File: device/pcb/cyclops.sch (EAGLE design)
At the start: 193 parts, among them Q1 NDS351AN, Q2 NDS351AN, Q3 NDS351AN, Q4 IRF510, U1 MCP4921, U10 LT1880, U11 ZXTD, U12 DG9421, U13 THS4281, U14 ZXTD, U15 MAX4564, U16 OPA1664, U2 LT1764A, U3 BD00FC0WEFJ, U4 LTM8020, U5 LT1931, U6 TPS72325, U7 TLV3701, U8 LT1711, U9 ADR03

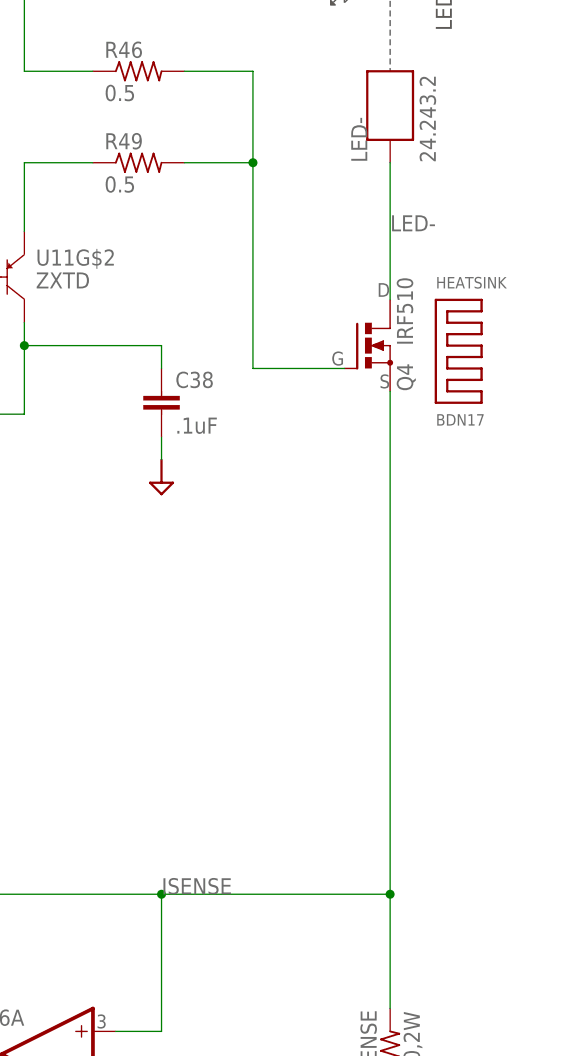
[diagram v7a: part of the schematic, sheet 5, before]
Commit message: Thermal fixes after testing.
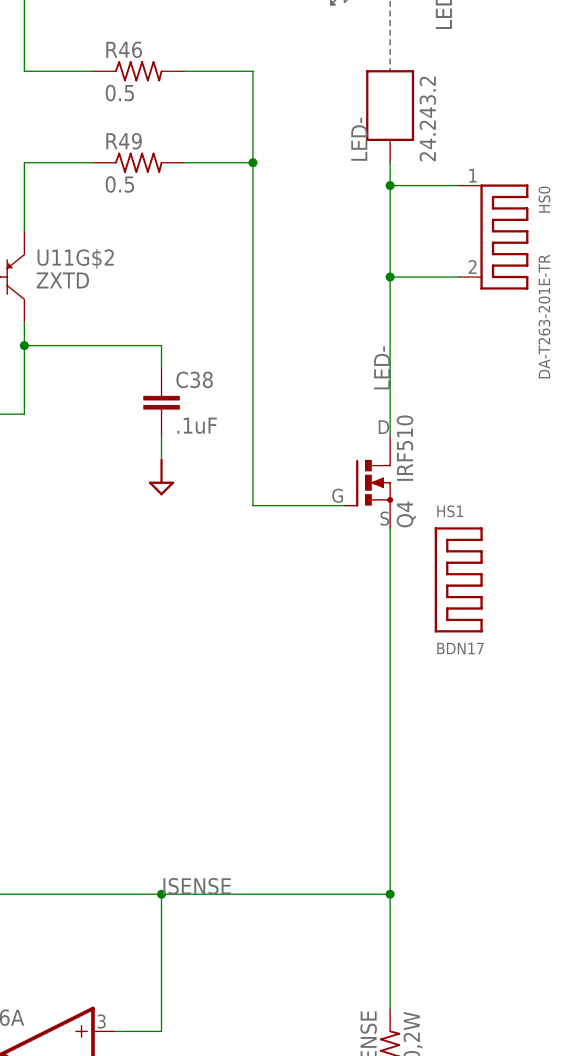
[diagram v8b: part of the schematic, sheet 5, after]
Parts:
- removed HEATSINK: BDN17, jonnew:HEATSINK_BDN17
- added HS0: DA-T263-201E-TR, jonnew:D-SERIES-HEATSINK_DA-T263-201E-TR
- added HS1: BDN17, jonnew:HEATSINK_BDN17
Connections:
- net LED-: now also HS0.P$1, HS0.P$3
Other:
- moved on the sheet: Q4
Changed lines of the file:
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@@
 <?xml version="1.0" encoding="utf-8"?>
 <!DOCTYPE eagle SYSTEM "eagle.dtd">
-<eagle version="6.6.0">
+<eagle version="6.5.0">
 <drawing>
 <settings>
@@
 <part name="R37" library="cyclops" deviceset="R" device="_0603" value="1k"/>
 <part name="U$44" library="cyclops" deviceset="GND2" device=""/>
-<part name="HEATSINK" library="jonnew" deviceset="HEATSINK" device="_BDN17" value="BDN17"/>
+<part name="HS1" library="jonnew" deviceset="HEATSINK" device="_BDN17" value="BDN17"/>
 <part name="R40" library="cyclops" deviceset="R" device="_0603" value="0"/>
 <part name="R42" library="cyclops" deviceset="R" device="_0603"/>
@@
 <part name="U$46" library="cyclops" deviceset="GND2" device=""/>
 <part name="U$69" library="cyclops" deviceset="GND2" device=""/>
+<part name="HS0" library="jonnew" deviceset="D-SERIES-HEATSINK" device="_DA-T263-201E-TR" value="DA-T263-201E-TR"/>
 </parts>
 <sheets>
@@
 </instance>
 <instance part="FRAME4" gate="G$1" x="-91.44" y="-58.42"/>
-<instance part="Q4" gate="G$1" x="162.56" y="73.66" smashed="yes">
-<attribute name="NAME" x="167.64" y="68.58" size="1.778" layer="95" rot="R90"/>
-<attribute name="VALUE" x="167.64" y="73.66" size="1.778" layer="96" rot="R90"/>
+<instance part="Q4" gate="G$1" x="162.56" y="58.42" smashed="yes">
+<attribute name="NAME" x="167.64" y="53.34" size="1.778" layer="95" rot="R90"/>
+<attribute name="VALUE" x="167.64" y="58.42" size="1.778" layer="96" rot="R90"/>
 </instance>
 <instance part="C46" gate="C" x="-17.78" y="-10.16"/>
@@
 <instance part="P-1" gate="1" x="-38.1" y="-20.32"/>
 <instance part="R50" gate="R" x="-22.86" y="88.9" rot="R90"/>
-<instance part="HEATSINK" gate="G$1" x="170.18" y="78.74" smashed="yes" rot="R270">
-<attribute name="NAME" x="170.18" y="80.01" size="1.27" layer="95"/>
-<attribute name="VALUE" x="170.18" y="64.77" size="1.27" layer="96"/>
+<instance part="HS1" gate="G$1" x="170.18" y="53.34" smashed="yes" rot="R270">
+<attribute name="NAME" x="170.18" y="54.61" size="1.27" layer="95"/>
+<attribute name="VALUE" x="170.18" y="39.37" size="1.27" layer="96"/>
 </instance>
 <instance part="R40" gate="R" x="-25.4" y="134.62" rot="R180"/>
@@
 <instance part="U$46" gate="G$1" x="139.7" y="58.42" rot="MR0"/>
 <instance part="U$69" gate="G$1" x="139.7" y="119.38" rot="MR0"/>
+<instance part="HS0" gate="G$1" x="175.26" y="91.44" rot="R270"/>
 </instances>
 <busses>
@@
 <wire x1="142.24" y1="104.14" x2="149.86" y2="104.14" width="0.1524" layer="91"/>
 <pinref part="Q4" gate="G$1" pin="G"/>
-<wire x1="149.86" y1="71.12" x2="160.02" y2="71.12" width="0.1524" layer="91"/>
+<wire x1="149.86" y1="55.88" x2="160.02" y2="55.88" width="0.1524" layer="91"/>
 <wire x1="149.86" y1="104.14" x2="149.86" y2="93.98" width="0.1524" layer="91"/>
 <pinref part="R49" gate="R" pin="2"/>
 <wire x1="149.86" y1="93.98" x2="142.24" y2="93.98" width="0.1524" layer="91"/>
 <junction x="149.86" y="93.98"/>
-<wire x1="149.86" y1="71.12" x2="149.86" y2="93.98" width="0.1524" layer="91"/>
+<wire x1="149.86" y1="55.88" x2="149.86" y2="93.98" width="0.1524" layer="91"/>
 </segment>
 </net>
@@
 <pinref part="LED-" gate="G$1" pin="1"/>
 <pinref part="Q4" gate="G$1" pin="D"/>
-<wire x1="165.1" y1="93.98" x2="165.1" y2="78.74" width="0.1524" layer="91"/>
-<label x="165.1" y="86.36" size="1.778" layer="95"/>
+<wire x1="165.1" y1="93.98" x2="165.1" y2="91.44" width="0.1524" layer="91"/>
+<label x="165.1" y="68.58" size="1.778" layer="95" rot="R90"/>
+<pinref part="HS0" gate="G$1" pin="P$1"/>
+<wire x1="165.1" y1="91.44" x2="165.1" y2="81.28" width="0.1524" layer="91"/>
+<wire x1="165.1" y1="81.28" x2="165.1" y2="63.5" width="0.1524" layer="91"/>
+<wire x1="172.72" y1="91.44" x2="165.1" y2="91.44" width="0.1524" layer="91"/>
+<junction x="165.1" y="91.44"/>
+<pinref part="HS0" gate="G$1" pin="P$3"/>
+<wire x1="172.72" y1="81.28" x2="165.1" y2="81.28" width="0.1524" layer="91"/>
+<junction x="165.1" y="81.28"/>
 </segment>
 </net>
@@
 <label x="139.7" y="12.7" size="1.778" layer="95"/>
 <pinref part="Q4" gate="G$1" pin="S"/>
-<wire x1="165.1" y1="68.58" x2="165.1" y2="12.7" width="0.1524" layer="91"/>
+<wire x1="165.1" y1="53.34" x2="165.1" y2="12.7" width="0.1524" layer="91"/>
 <junction x="165.1" y="12.7"/>
 </segment>
